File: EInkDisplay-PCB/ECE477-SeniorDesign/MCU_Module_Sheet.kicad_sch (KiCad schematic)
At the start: 18 parts, among them SW1 SW_Push_Dual_x2, U3 STM32L496ZGTxP

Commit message: Changes
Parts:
- added R1: 10k, symbol Device:R_Small
- added SWBOOT0: SW_SPDT, symbol Switch:SW_SPDT
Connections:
- net +3.3V: now also SWBOOT0.3 (C)
- net GND: now also SWBOOT0.1 (A)
- net at U3.137 (PH3): now also R1.2
- new net: R1.1, SWBOOT0.2 (B)

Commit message: push
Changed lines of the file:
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@@
 		)
 	)
-	(global_label "USART1_RX"
+	(hierarchical_label "SPI1_MOSI"
 		(shape input)
-		(at 238.76 80.01 0)
-		(fields_autoplaced yes)
+		(at 238.76 110.49 0)
 		(effects
 			(font
@@
 			(justify left)
 		)
-		(property "Intersheetrefs" "${INTERSHEET_REFS}"
-			(at 252.268 80.01 0)
-			(effects
-				(font
-					(size 1.27 1.27)
-				)
-				(justify left)
-				(hide yes)
-			)
-		)
 	)
-	(global_label "SPI1_SCK"
+	(hierarchical_label "USART1_RX"
 		(shape input)
-		(at 238.76 105.41 0)
-		(fields_autoplaced yes)
+		(at 238.76 80.01 0)
 		(effects
 			(font
@@
 			(justify left)
 		)
-		(property "Intersheetrefs" "${INTERSHEET_REFS}"
-			(at 250.7561 105.41 0)
-			(effects
-				(font
-					(size 1.27 1.27)
-				)
-				(justify left)
-				(hide yes)
-			)
-		)
 	)
-	(global_label "SPI1_MOSI"
+	(hierarchical_label "SPI1_SCK"
 		(shape input)
-		(at 238.76 110.49 0)
-		(fields_autoplaced yes)
+		(at 238.76 105.41 0)
 		(effects
 			(font
@@
 			(justify left)
 		)
-		(property "Intersheetrefs" "${INTERSHEET_REFS}"
-			(at 251.6028 110.49 0)
-			(effects
-				(font
-					(size 1.27 1.27)
-				)
-				(justify left)
-				(hide yes)
-			)
-		)
 	)
-	(global_label "USART1_TX"
+	(hierarchical_label "USART1_TX"
 		(shape input)
 		(at 238.76 77.47 0)
-		(fields_autoplaced yes)
 		(effects
 			(font
@@
 			(justify left)
 		)
-		(property "Intersheetrefs" "${INTERSHEET_REFS}"
-			(at 251.9656 77.47 0)
-			(effects
-				(font
-					(size 1.27 1.27)
-				)
-				(justify left)
-				(hide yes)
-			)
-		)
 	)

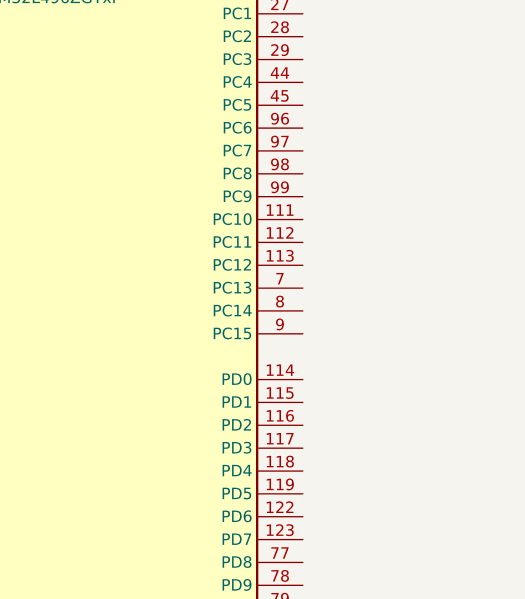
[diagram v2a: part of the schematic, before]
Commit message: Adding SD
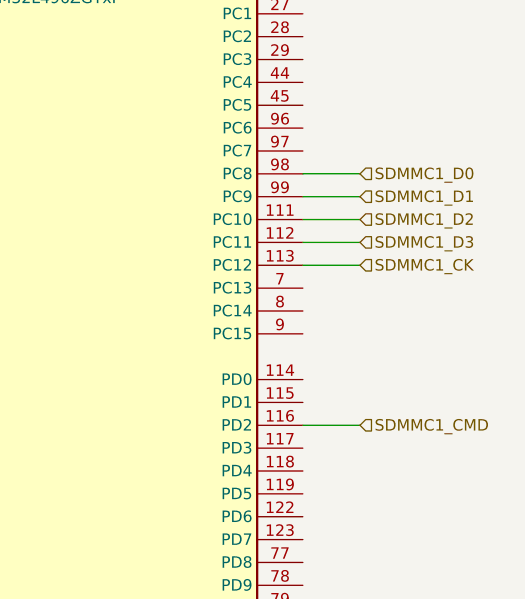
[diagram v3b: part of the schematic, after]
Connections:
- net SDMMC1_D2: now reaches U3.111 (PC10)
- net SDMMC1_D3: now reaches U3.112 (PC11)
- net SDMMC1_CK: now reaches U3.113 (PC12)
- net SDMMC1_CMD: now reaches U3.116 (PD2)
- net SDMMC1_D0: now reaches U3.98 (PC8)
- net SDMMC1_D1: now reaches U3.99 (PC9)
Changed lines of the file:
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@@
+	(wire
+		(pts
+			(xy 232.41 158.75) (xy 238.76 158.75)
+		)
+		(stroke
+			(width 0)
+			(type default)
+		)
+	)
 	(wire
 		(pts
@@
 	(wire
 		(pts
+			(xy 232.41 166.37) (xy 238.76 166.37)
+		)
+		(stroke
+			(width 0)
+			(type default)
+		)
+	)
+	(wire
+		(pts
 			(xy 199.39 36.83) (xy 203.2 36.83)
 		)
@@
 	(wire
 		(pts
+			(xy 232.41 168.91) (xy 238.76 168.91)
+		)
+		(stroke
+			(width 0)
+			(type default)
+		)
+	)
+	(wire
+		(pts
 			(xy 201.93 232.41) (xy 201.93 229.87)
 		)
@@
 	(wire
 		(pts
+			(xy 232.41 163.83) (xy 238.76 163.83)
+		)
+		(stroke
+			(width 0)
+			(type default)
+		)
+	)
+	(wire
+		(pts
 			(xy 189.23 41.91) (xy 189.23 44.45)
 		)
@@
 	(wire
 		(pts
+			(xy 232.41 161.29) (xy 238.76 161.29)
+		)
+		(stroke
+			(width 0)
+			(type default)
+		)
+	)
+	(wire
+		(pts
 			(xy 128.27 64.77) (xy 128.27 69.85)
 		)
@@
 		(pts
 			(xy 219.71 41.91) (xy 217.17 41.91)
+		)
+		(stroke
+			(width 0)
+			(type default)
+		)
+	)
+	(wire
+		(pts
+			(xy 238.76 186.69) (xy 232.41 186.69)
 		)
 		(stroke
@@
 		)
 	)
+	(hierarchical_label "SDMMC1_D2"
+		(shape input)
+		(at 238.76 163.83 0)
+		(effects
+			(font
+				(size 1.27 1.27)
+			)
+			(justify left)
+		)
+	)
 	(hierarchical_label "SPI1_MOSI"
 		(shape input)
@@
 		)
 	)
+	(hierarchical_label "SDMMC1_D0"
+		(shape input)
+		(at 238.76 158.75 0)
+		(effects
+			(font
+				(size 1.27 1.27)
+			)
+			(justify left)
+		)
+	)
+	(hierarchical_label "SDMMC1_CMD"
+		(shape input)
+		(at 238.76 186.69 0)
+		(effects
+			(font
+				(size 1.27 1.27)
+			)
+			(justify left)
+		)
+	)
 	(hierarchical_label "USART1_RX"
 		(shape input)
@@
 		)
 	)
+	(hierarchical_label "SDMMC1_D3"
+		(shape input)
+		(at 238.76 166.37 0)
+		(effects
+			(font
+				(size 1.27 1.27)
+			)
+			(justify left)
+		)
+	)
+	(hierarchical_label "SDMMC1_D1"
+		(shape input)
+		(at 238.76 161.29 0)
+		(effects
+			(font
+				(size 1.27 1.27)
+			)
+			(justify left)
+		)
+	)
 	(hierarchical_label "SPI1_SCK"
 		(shape input)
@@
 		(effects
 			(font
+				(size 1.27 1.27)
+			)
+			(justify left)
+		)
+	)
+	(hierarchical_label "SDMMC1_CK"
+		(shape input)
+		(at 238.76 168.91 0)
+		(effects
+			(font

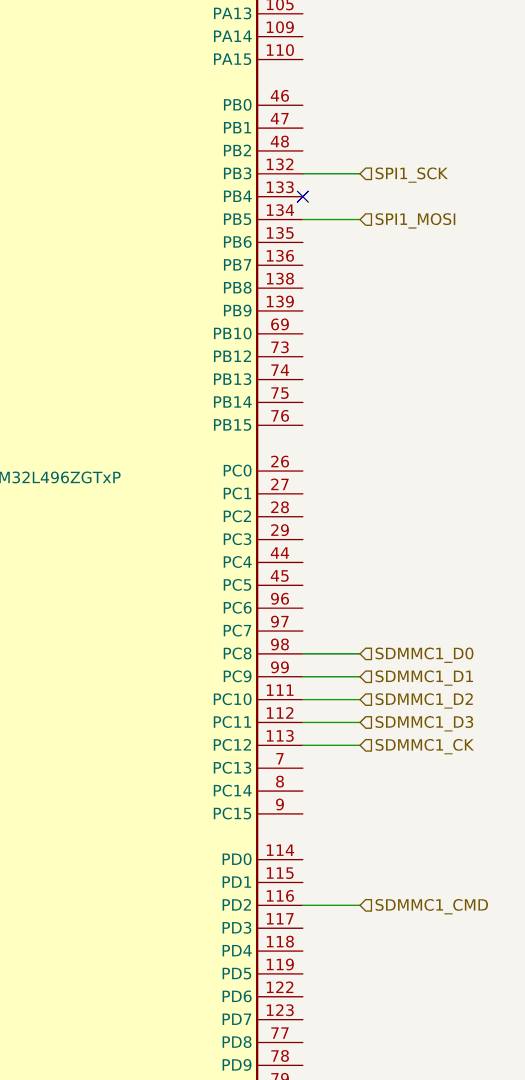
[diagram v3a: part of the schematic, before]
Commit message: Fixing SD w SPI
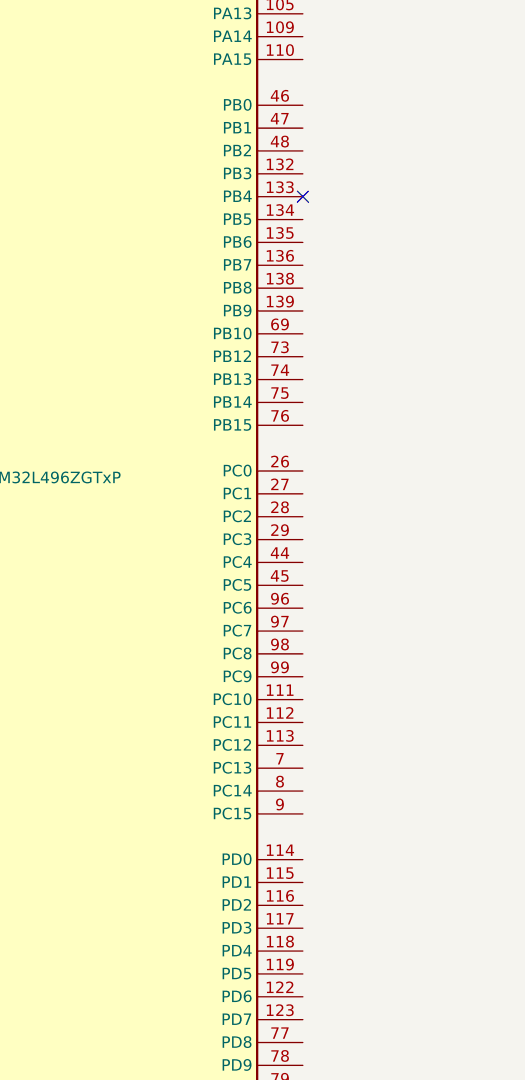
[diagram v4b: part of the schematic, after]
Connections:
- net SDMMC1_CK: no longer names the net of U3.113 (PC12)
- net SDMMC1_CMD: no longer names the net of U3.116 (PD2)
- net SDMMC1_D0: no longer names the net of U3.98 (PC8)
- net SDMMC1_D1: no longer names the net of U3.99 (PC9)
- net SDMMC1_D2: no longer names the net of U3.111 (PC10)
- net SDMMC1_D3: no longer names the net of U3.112 (PC11)
- net SPI1_MOSI: no longer names the net of U3.134 (PB5)
- net SPI1_SCK: no longer names the net of U3.132 (PB3)
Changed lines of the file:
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@@
-	(wire
-		(pts
-			(xy 232.41 158.75) (xy 238.76 158.75)
-		)
-		(stroke
-			(width 0)
-			(type default)
-		)
-	)
 	(wire
 		(pts
@@
 	(wire
 		(pts
-			(xy 232.41 105.41) (xy 238.76 105.41)
-		)
-		(stroke
-			(width 0)
-			(type default)
-		)
-	)
-	(wire
-		(pts
 			(xy 223.52 36.83) (xy 228.6 36.83)
 		)
@@
 	(wire
 		(pts
-			(xy 232.41 166.37) (xy 238.76 166.37)
-		)
-		(stroke
-			(width 0)
-			(type default)
-		)
-	)
-	(wire
-		(pts
 			(xy 199.39 36.83) (xy 203.2 36.83)
 		)
@@
 	(wire
 		(pts
-			(xy 232.41 168.91) (xy 238.76 168.91)
-		)
-		(stroke
-			(width 0)
-			(type default)
-		)
-	)
-	(wire
-		(pts
 			(xy 201.93 232.41) (xy 201.93 229.87)
 		)
@@
 	(wire
 		(pts
-			(xy 232.41 163.83) (xy 238.76 163.83)
-		)
-		(stroke
-			(width 0)
-			(type default)
-		)
-	)
-	(wire
-		(pts
 			(xy 189.23 41.91) (xy 189.23 44.45)
 		)
@@
 	(wire
 		(pts
-			(xy 232.41 161.29) (xy 238.76 161.29)
-		)
-		(stroke
-			(width 0)
-			(type default)
-		)
-	)
-	(wire
-		(pts
 			(xy 128.27 64.77) (xy 128.27 69.85)
 		)
@@
 	(wire
 		(pts
-			(xy 238.76 186.69) (xy 232.41 186.69)
-		)
-		(stroke
-			(width 0)
-			(type default)
-		)
-	)
-	(wire
-		(pts
 			(xy 219.71 44.45) (xy 219.71 41.91)
 		)
@@
 		(pts
 			(xy 184.15 36.83) (xy 184.15 41.91)
-		)
-		(stroke
-			(width 0)
-			(type default)
-		)
-	)
-	(wire
-		(pts
-			(xy 232.41 110.49) (xy 238.76 110.49)
 		)
 		(stroke
@@
 		)
 	)
-	(hierarchical_label "SDMMC1_D2"
-		(shape input)
-		(at 238.76 163.83 0)
-		(effects
-			(font
-				(size 1.27 1.27)
-			)
-			(justify left)
-		)
-	)
-	(hierarchical_label "SPI1_MOSI"
-		(shape input)
-		(at 238.76 110.49 0)
-		(effects
-			(font
-				(size 1.27 1.27)
-			)
-			(justify left)
-		)
-	)
-	(hierarchical_label "SDMMC1_D0"
-		(shape input)
-		(at 238.76 158.75 0)
-		(effects
-			(font
-				(size 1.27 1.27)
-			)
-			(justify left)
-		)
-	)
-	(hierarchical_label "SDMMC1_CMD"
-		(shape input)
-		(at 238.76 186.69 0)
-		(effects
-			(font
-				(size 1.27 1.27)
-			)
-			(justify left)
-		)
-	)
 	(hierarchical_label "USART1_RX"
 		(shape input)
@@
 		(effects
 			(font
-				(size 1.27 1.27)
-			)
-			(justify left)
-		)
-	)
-	(hierarchical_label "SDMMC1_D3"
-		(shape input)
-		(at 238.76 166.37 0)
-		(effects
-			(font
-				(size 1.27 1.27)
-			)
-			(justify left)
-		)
-	)
-	(hierarchical_label "SDMMC1_D1"
-		(shape input)
-		(at 238.76 161.29 0)
-		(effects
-			(font
-				(size 1.27 1.27)
-			)
-			(justify left)
-		)
-	)
-	(hierarchical_label "SPI1_SCK"
-		(shape input)
-		(at 238.76 105.41 0)
-		(effects
-			(font
-				(size 1.27 1.27)
-			)
-			(justify left)
-		)
-	)
-	(hierarchical_label "SDMMC1_CK"
-		(shape input)
-		(at 238.76 168.91 0)
-		(effects
-			(font

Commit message: push
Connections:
- net SD_GPIO: now reaches U3.100 (PA8)
- net SPI2_NSS: now reaches U3.139 (PB9)
- net SPI2_SCK: now reaches U3.69 (PB10)
- net SPI2_MISO: now reaches U3.75 (PB14)
- net SPI2_MOSI: now reaches U3.76 (PB15)
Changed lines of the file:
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@@
+	(wire
+		(pts
+			(xy 232.41 120.65) (xy 241.3 120.65)
+		)
+		(stroke
+			(width 0)
+			(type default)
+		)
+	)
 	(wire
 		(pts
@@
 	(wire
 		(pts
+			(xy 232.41 123.19) (xy 241.3 123.19)
+		)
+		(stroke
+			(width 0)
+			(type default)
+		)
+	)
+	(wire
+		(pts
 			(xy 191.77 31.75) (xy 195.58 31.75)
 		)
@@
 	(wire
 		(pts
+			(xy 232.41 133.35) (xy 241.3 133.35)
+		)
+		(stroke
+			(width 0)
+			(type default)
+		)
+	)
+	(wire
+		(pts
 			(xy 238.76 31.75) (xy 243.84 31.75)
 		)
@@
 	(wire
 		(pts
+			(xy 232.41 74.93) (xy 238.76 74.93)
+		)
+		(stroke
+			(width 0)
+			(type default)
+		)
+	)
+	(wire
+		(pts
 			(xy 184.15 36.83) (xy 184.15 41.91)
+		)
+		(stroke
+			(width 0)
+			(type default)
+		)
+	)
+	(wire
+		(pts
+			(xy 232.41 130.81) (xy 241.3 130.81)
 		)
 		(stroke
@@
 		)
 	)
+	(hierarchical_label "SPI2_MISO"
+		(shape input)
+		(at 241.3 130.81 0)
+		(effects
+			(font
+				(size 1.27 1.27)
+			)
+			(justify left)
+		)
+	)
 	(hierarchical_label "USART1_RX"
 		(shape input)
@@
 		(effects
 			(font
+				(size 1.27 1.27)
+			)
+			(justify left)
+		)
+	)
+	(hierarchical_label "SPI2_NSS"
+		(shape input)
+		(at 241.3 120.65 0)
+		(effects
+			(font
+				(size 1.27 1.27)
+			)
+			(justify left)
+		)
+	)
+	(hierarchical_label "SPI2_MOSI"
+		(shape input)
+		(at 241.3 133.35 0)
+		(effects
+			(font
+				(size 1.27 1.27)
+			)
+			(justify left)
+		)
+	)
+	(hierarchical_label "SD_GPIO"
+		(shape input)
+		(at 238.76 74.93 0)
+		(effects
+			(font
+				(size 1.27 1.27)
+			)
+			(justify left)
+		)
+	)
+	(hierarchical_label "SPI2_SCK"
+		(shape input)
+		(at 241.3 123.19 0)
+		(effects
+			(font

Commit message: Changes
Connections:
- net Eink_D/C: now reaches U3.103 (PA11)
- net Eink_RST: now reaches U3.104 (PA12)
- net button1: now reaches U3.29 (PC3)
- net SPI1_NSS: now reaches U3.40 (PA4)
- net SPI1_SCK: now reaches U3.41 (PA5)
- net Eink_Busy: now reaches U3.42 (PA6)
- net SPI1_MOSI: now reaches U3.43 (PA7)
- net button2: now reaches U3.44 (PC4)
- net button3: now reaches U3.45 (PC5)
- no-connect marks 3 -> 5
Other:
- note added: "BOOT0"
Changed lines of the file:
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@@
+	)
+	(no_connect
+		(at 166.37 69.85)
 	)
 	(no_connect
@@
 	)
 	(no_connect
+		(at 166.37 67.31)
+	)
+	(no_connect
 		(at 209.55 44.45)
 	)
@@
 	(wire
 		(pts
+			(xy 232.41 72.39) (xy 238.76 72.39)
+		)
+		(stroke
+			(width 0)
+			(type default)
+		)
+	)
+	(wire
+		(pts
 			(xy 232.41 120.65) (xy 241.3 120.65)
 		)
@@
 	(wire
 		(pts
+			(xy 232.41 151.13) (xy 241.3 151.13)
+		)
+		(stroke
+			(width 0)
+			(type default)
+		)
+	)
+	(wire
+		(pts
+			(xy 232.41 64.77) (xy 238.76 64.77)
+		)
+		(stroke
+			(width 0)
+			(type default)
+		)
+	)
+	(wire
+		(pts
 			(xy 196.85 41.91) (xy 196.85 44.45)
 		)
@@
 	(wire
 		(pts
+			(xy 232.41 148.59) (xy 241.3 148.59)
+		)
+		(stroke
+			(width 0)
+			(type default)
+		)
+	)
+	(wire
+		(pts
 			(xy 217.17 41.91) (xy 214.63 41.91)
 		)
@@
 	(wire
 		(pts
+			(xy 232.41 146.05) (xy 241.3 146.05)
+		)
+		(stroke
+			(width 0)
+			(type default)
+		)
+	)
+	(wire
+		(pts
 			(xy 128.27 64.77) (xy 128.27 69.85)
 		)
@@
 	(wire
 		(pts
+			(xy 232.41 85.09) (xy 238.76 85.09)
+		)
+		(stroke
+			(width 0)
+			(type default)
+		)
+	)
+	(wire
+		(pts
 			(xy 195.58 31.75) (xy 199.39 31.75)
 		)
@@
 	(wire
 		(pts
+			(xy 232.41 82.55) (xy 238.76 82.55)
+		)
+		(stroke
+			(width 0)
+			(type default)
+		)
+	)
+	(wire
+		(pts
 			(xy 238.76 31.75) (xy 243.84 31.75)
 		)
@@
 	(wire
 		(pts
+			(xy 232.41 69.85) (xy 238.76 69.85)
+		)
+		(stroke
+			(width 0)
+			(type default)
+		)
+	)
+	(wire
+		(pts
 			(xy 213.36 36.83) (xy 218.44 36.83)
 		)
@@
 	(wire
 		(pts
+			(xy 232.41 67.31) (xy 238.76 67.31)
+		)
+		(stroke
+			(width 0)
+			(type default)
+		)
+	)
+	(wire
+		(pts
 			(xy 232.41 74.93) (xy 238.76 74.93)
 		)
@@
 			(width 0)
 			(type default)
+		)
+	)
+	(text "BOOT0\n"
+		(exclude_from_sim no)
+		(at 162.306 74.422 0)
+		(effects
+			(font
+				(size 1.27 1.27)
+			)
 		)
 	)
@@
 		)
 	)
+	(hierarchical_label "Eink_Busy"
+		(shape input)
+		(at 238.76 69.85 0)
+		(effects
+			(font
+				(size 1.27 1.27)
+			)
+			(justify left)
+		)
+	)
+	(hierarchical_label "SPI1_SCK"
+		(shape input)
+		(at 238.76 67.31 0)
+		(effects
+			(font
+				(size 1.27 1.27)
+			)
+			(justify left)
+		)
+	)
 	(hierarchical_label "SPI2_MISO"
 		(shape input)
@@
 		)
 	)
+	(hierarchical_label "button3"
+		(shape input)
+		(at 241.3 151.13 0)
+		(effects
+			(font
+				(size 1.27 1.27)
+			)
+			(justify left)
+		)
+	)
+	(hierarchical_label "button2"
+		(shape input)
+		(at 241.3 148.59 0)
+		(effects
+			(font
+				(size 1.27 1.27)
+			)
+			(justify left)
+		)
+	)
 	(hierarchical_label "USART1_RX"
 		(shape input)
@@
 		)
 	)
+	(hierarchical_label "SPI1_NSS"
+		(shape input)
+		(at 238.76 64.77 0)
+		(effects
+			(font
+				(size 1.27 1.27)
+			)
+			(justify left)
+		)
+	)
+	(hierarchical_label "Eink_RST"
+		(shape input)
+		(at 238.76 85.09 0)
+		(effects
+			(font
+				(size 1.27 1.27)
+			)
+			(justify left)
+		)
+	)
 	(hierarchical_label "SPI2_NSS"
 		(shape input)
@@
 		(effects
 			(font
+				(size 1.27 1.27)
+			)
+			(justify left)
+		)
+	)
+	(hierarchical_label "button1"
+		(shape input)
+		(at 241.3 146.05 0)
+		(effects
+			(font
+				(size 1.27 1.27)
+			)
+			(justify left)
+		)
+	)
+	(hierarchical_label "Eink_D{slash}C"
+		(shape input)
+		(at 238.76 82.55 0)
+		(effects
+			(font
+				(size 1.27 1.27)
+			)
+			(justify left)
+		)
+	)
+	(hierarchical_label "SPI1_MOSI"
+		(shape input)
+		(at 238.76 72.39 0)
+		(effects
+			(font

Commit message: Changes
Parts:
- added C28, C29: 20pF, symbol Device:C_Small
- added Y1: 32.768kHz, symbol Device:Crystal
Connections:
- net GND: now also C28.1, C29.1
- net at U3.23 (PH0): now also C28.2, Y1.1
- net at U3.24 (PH1): now also C29.2, Y1.2
- no-connect marks 5 -> 3
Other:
- note added: "enter bootloader mode"
- note added: "force reset"
- moved on the sheet: R1, SWBOOT0

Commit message: push
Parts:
- added TP15: NSRT, symbol Connector:TestPoint
- added TP16: BOOT0, symbol Connector:TestPoint
- R1: footprint (none) -> Resistor_SMD:R_0603_1608Metric_Pad0.98x0.95mm_HandSolder
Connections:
- net +3.3V: now also U3.6 (VBAT)
- net GND: now also U3.107 (VSS), U3.120 (VSS), U3.130 (VSS), U3.143 (VSS), U3.16 (VSS), U3.30 (VSSA), U3.38 (VSS), U3.51 (VSS), U3.61 (VSS), U3.71 (VSS), U3.83 (VSS), U3.94 (VSS)
- net NRST: now also TP15.1
- net at R1.2, U3.137 (PH3): now also TP16.1
- no-connect marks 3 -> 96
